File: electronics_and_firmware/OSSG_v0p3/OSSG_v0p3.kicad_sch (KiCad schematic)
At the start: 61 parts, among them IC1 DW01A, J1 USB_B_Micro, Q1 FS8205A, Q2 Q_NPN_BEC, Q3 Q_NPN_BEC, SW1 SW_SPST, U1 ESP32-PICO-D4, U2 TP4056, U3 XC6222B331MRG, U4 FT232RQ

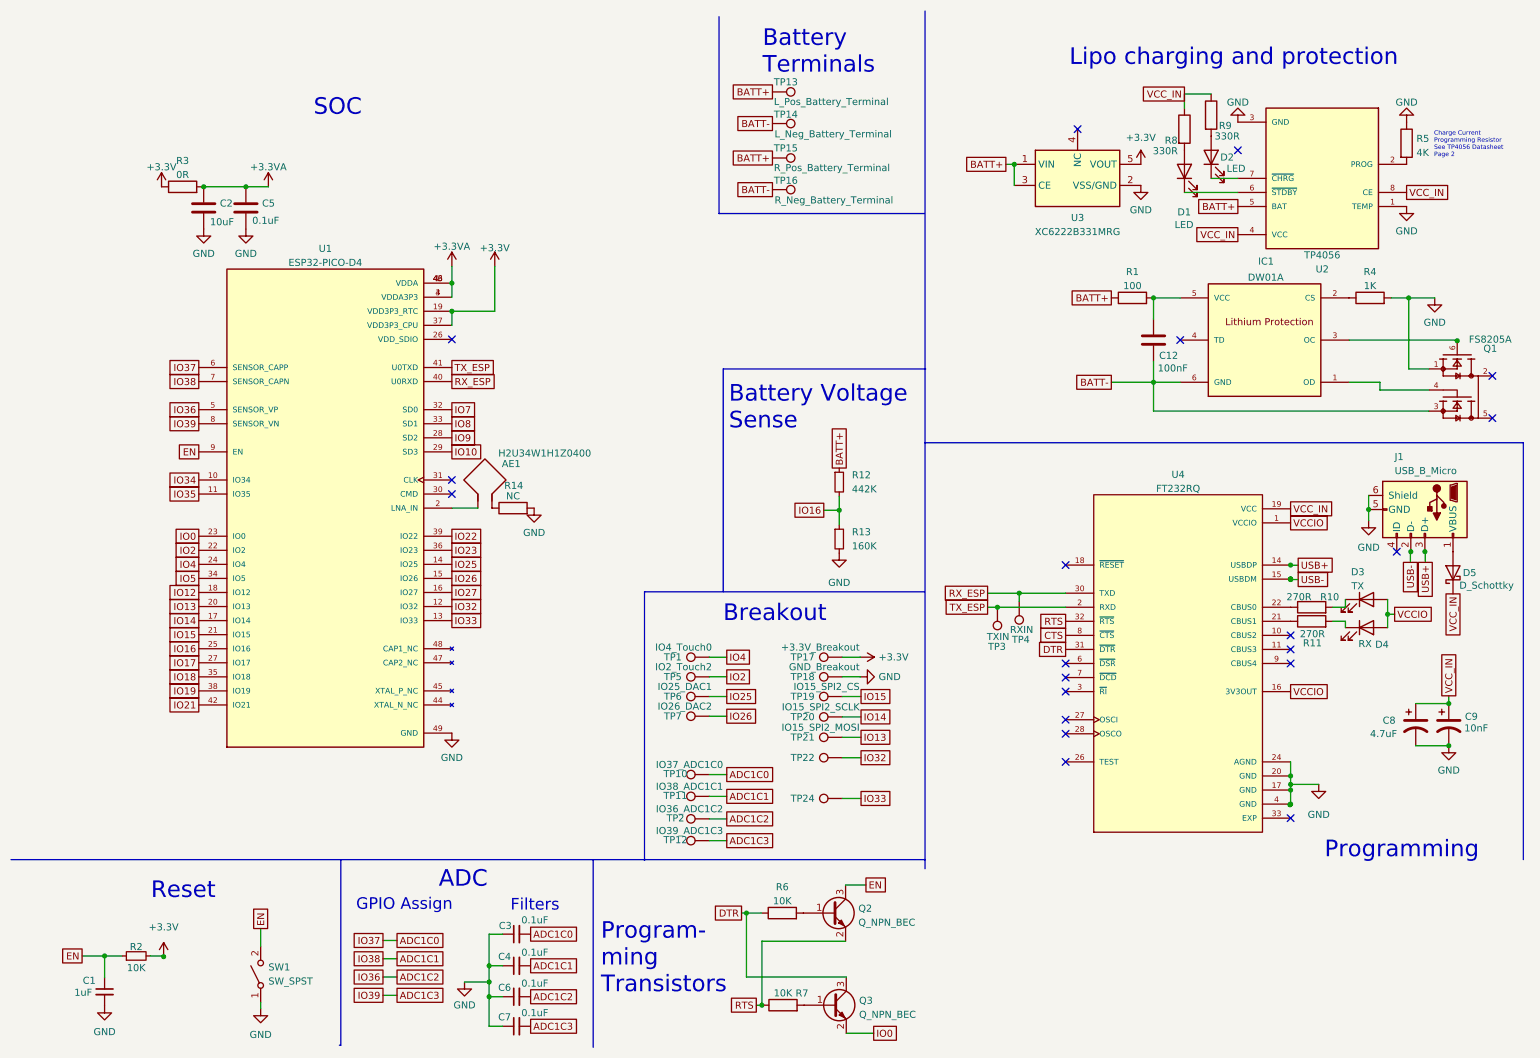
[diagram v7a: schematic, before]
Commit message: add voltage supervisor, go back to PRO_OB_440 antenna, more layout
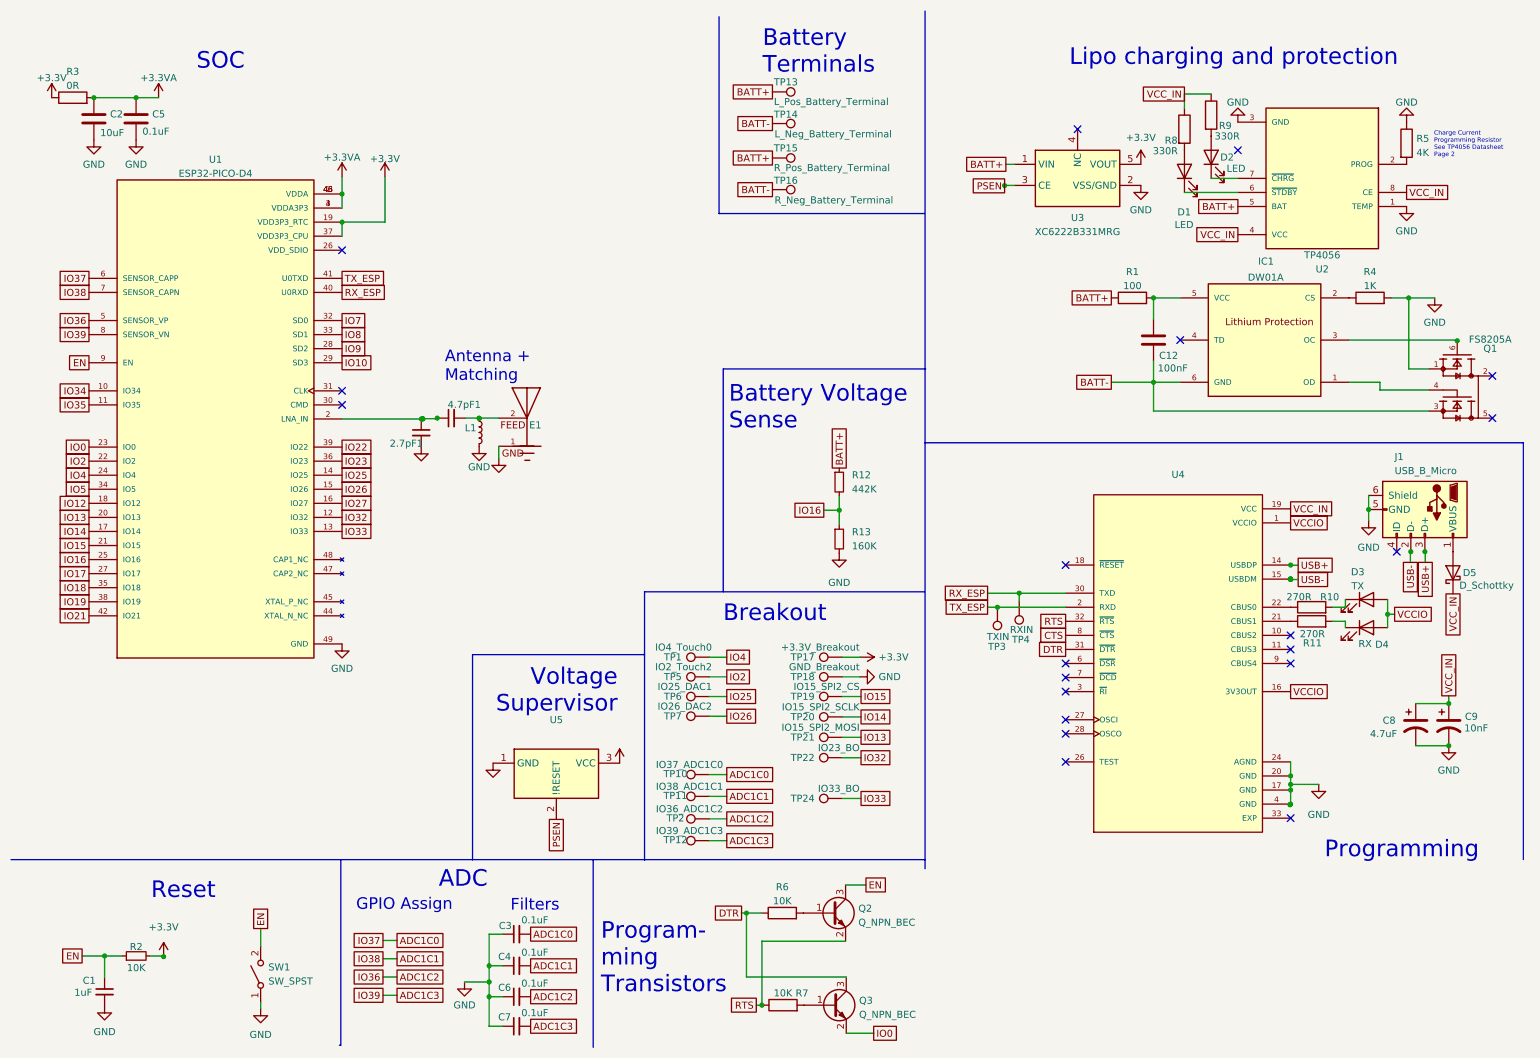
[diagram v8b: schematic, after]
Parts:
- removed AE1: H2U34W1H1Z0400, Resistor_SMD:R_1206_3216Metric, symbol Device:Antenna_Loop
- removed R14: NC, Resistor_SMD:R_0402_1005Metric, symbol Device:R
- added 2.7pF1, 4.7pF1: (no value), symbol Device:C_Small
- added E1: (no value), symbol OSSG_components_lib:PRO-OB-440
- added L1: (no value), symbol Device:L_Small
- added U5: (no value), Package_TO_SOT_SMD:SOT-23, symbol OSSG_components_lib:APX803L-29SA-7
- TP22: value (none) -> IO23_BO
- TP24: value (none) -> IO33_BO
- U4: value FT232RQ -> (none); footprint Package_DFN_QFN:QFN-32-1EP_5x5mm_P0.5mm_EP3.1x3.1mm -> (none)
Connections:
- net +3V3: now also U5.3 (VCC)
- net BATT+: no longer U3.3 (CE)
- net GND: now also 2.7pF1.2, E1.1 (GND), L1.2, U5.1 (GND)
- net at U1.2 (LNA_IN): now also 2.7pF1.1, 4.7pF1.1
- new net: 4.7pF1.2, E1.2 (FEED), L1.1
- new net PSEN: U3.3 (CE), U5.2 (!RESET)
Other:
- note added: "Antenna + Matching"
- note added: "Voltage Supervisor"
- moved on the sheet: C2, C5, R3, U1
